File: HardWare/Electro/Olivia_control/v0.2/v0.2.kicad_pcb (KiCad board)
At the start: 2 copper layers, 90 x 100 mm, 49 parts, among them J1 PROG, J10 Motor_B, J11 I2C, J12 DAC, J13 UART2, J14 TRIAC OUT_A, J15 TRIAC OUT_B, J16 220V IN, J17 In12V, J2 Input1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

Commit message: Añadida serigrafía para fabricación industrial.
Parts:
- J17: value In12V -> Input 12Vcc max
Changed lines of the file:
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@@
 		(tags "resistor handsolder")
 		(property "Reference" "R2"
-			(at 0 -1.65 0)
+			(at 0.005398 1.74998 0)
 			(layer "F.SilkS")
 			(effects
@@
 		)
 		(property "Value" "10K"
-			(at 0 1.65 0)
-			(layer "F.Fab")
+			(at -2.576 1.804 0)
+			(layer "F.SilkS")
 			(effects
 				(font
@@
 		(tags "capacitor handsolder")
 		(property "Reference" "C5"
-			(at 0 -1.68 0)
+			(at -1.398 -1.862 0)
 			(layer "F.SilkS")
 			(effects
@@
 		)
 		(property "Value" "100nF"
-			(at 0 1.68 0)
-			(layer "F.Fab")
+			(at -4.954 -1.862 0)
+			(layer "F.SilkS")
 			(effects
 				(font
@@
 		(property "Value" "10uF"
 			(at 0 1.68 0)
-			(layer "F.Fab")
+			(layer "F.SilkS")
 			(effects
 				(font
@@
 		(tags "resistor handsolder")
 		(property "Reference" "R1"
-			(at 0 -1.65 0)
+			(at 0.352 1.648 0)
 			(layer "F.SilkS")
 			(effects
@@
 		)
 		(property "Value" "10K"
-			(at 0 1.65 0)
-			(layer "F.Fab")
+			(at -2.188 1.65 0)
+			(layer "F.SilkS")
 			(effects
 				(font
@@
 		)
 		(property "Value" "100nF"
-			(at -0.0375 -3.25 0)
-			(layer "F.Fab")
+			(at -0.0375 2.026 0)
+			(layer "F.SilkS")
 			(effects
 				(font
@@
 			)
 		)
-		(property "Value" "In12V"
-			(at -6.2 -5.5 90)
-			(layer "F.Fab")
+		(property "Value" "Input 12Vcc max"
+			(at 3.252 -0.316 180)
+			(layer "F.SilkS")
 			(effects
 				(font
@@
 		(property "Value" "10K"
 			(at 0 1.65 0)
-			(layer "F.Fab")
+			(layer "F.SilkS")
 			(effects
 				(font
@@
 		(property "Value" "ESP32-WROOM-32D"
 			(at 0 11.5 0)
-			(layer "F.Fab")
+			(layer "F.SilkS")
 			(effects
 				(font
@@
 		(tags "resistor handsolder")
 		(property "Reference" "R4"
-			(at 0 -1.65 0)
+			(at 0 1.668 0)
 			(layer "F.SilkS")
 			(effects
@@
 		)
 		(property "Value" "10K"
-			(at 0 2 0)
-			(layer "F.Fab")
+			(at -3.0665 1.668 0)
+			(layer "F.SilkS")
 			(effects
 				(font
@@
 		(tags "resistor handsolder")
 		(property "Reference" "R3"
-			(at 0 -1.65 0)
+			(at 0.003171 1.676848 0)
 			(layer "F.SilkS")
 			(effects
@@
 		)
 		(property "Value" "10K"
-			(at 0 1.65 0)
-			(layer "F.Fab")
+			(at -2.596 1.65 0)
+			(layer "F.SilkS")
 			(effects
 				(font
@@
 		(tags "ACDC-Converter 10W THT Hi-Link board mount module")
 		(property "Reference" "PS1"
-			(at -1.3 -12.39 0)
+			(at 38.0285 -12.774 0)
 			(layer "F.SilkS")
 			(effects
@@
 		)
 		(property "Value" "HLK-10M05"
-			(at -8.45 -1.7 0)
-			(layer "F.Fab")
+			(at 31.4245 -12.774 0)
+			(layer "F.SilkS")
 			(effects
 				(font
@@
 		(tags "capacitor handsolder")
 		(property "Reference" "C2"
-			(at 0 -1.68 0)
+			(at -1.498803 -1.68 0)
 			(layer "F.SilkS")
 			(effects
@@
 		)
 		(property "Value" "100nF"
-			(at 0 1.68 0)
-			(layer "F.Fab")
+			(at -5.004 -1.707953 0)
+			(layer "F.SilkS")
 			(effects
 				(font
@@
 		(tags "capacitor handsolder")
 		(property "Reference" "C3"
-			(at 0 -1.68 0)
+			(at -1.68726 -1.792 0)
 			(layer "F.SilkS")
 			(effects
@@
 		)
 		(property "Value" "100nF"
-			(at 0 1.68 0)
-			(layer "F.Fab")
+			(at -5.104 -1.792 0)
+			(layer "F.SilkS")
 			(effects
 				(font
@@
 		(tags "capacitor handsolder")
 		(property "Reference" "C4"
-			(at 0 -1.68 0)
+			(at -1.548 -1.68 0)
 			(layer "F.SilkS")
 			(effects
@@
 		)
 		(property "Value" "100nF"
-			(at 0 1.68 0)
-			(layer "F.Fab")
+			(at -5.104 -1.536 0)
+			(layer "F.SilkS")
 			(effects
 				(font
@@
 		(property "Value" "100nF"
 			(at 0 -1.68 90)
-			(layer "B.Fab")
+			(layer "B.SilkS")
 			(effects
 				(font
@@
 		(property "Value" "220"
 			(at 0 -1.65 0)
-			(layer "B.Fab")
+			(layer "B.SilkS")
 			(effects
 				(font
@@
 		(property "Value" "BTA16-800B"
 			(at 2.54 -2.5 90)
-			(layer "B.Fab")
+			(layer "B.SilkS")
 			(effects
 				(font
@@
 		(property "Value" "LED"
 			(at 2.54 -5.25 90)
-			(layer "B.Fab")
+			(layer "B.SilkS")
 			(effects
 				(font
@@
 		(property "Value" "4N25"
 			(at 0 -4.87 0)
-			(layer "B.Fab")
+			(layer "B.SilkS")
 			(effects
 				(font
@@
 		(property "Value" "BTA16-800B"
 			(at 2.54 -2.5 90)
-			(layer "B.Fab")
+			(layer "B.SilkS")
 			(effects
 				(font
@@
 		)
 		(property "Value" "TRIAC OUT_B"
-			(at 3.81 -11.2 0)
-			(layer "B.Fab")
+			(at 3.302 4.826 0)
+			(layer "B.SilkS")
 			(effects
 				(font
@@
 		)
 		(property "Value" "Input2"
-			(at 1.27 -5.25 90)
-			(layer "B.Fab")
+			(at 1.27 4.7825 90)
+			(layer "B.SilkS")
 			(effects
 				(font
@@
 		(tags "connector Molex SL vertical")
 		(property "Reference" "J11"
-			(at 3.81 3.75 90)
+			(at 6.822 -5.2 90)
 			(layer "B.SilkS")
 			(effects
@@
 		(property "Value" "I2C"
 			(at 3.81 -5.25 90)
-			(layer "B.Fab")
+			(layer "B.SilkS")
 			(effects
 				(font
@@
 		(property "Value" "Motor_A"
 			(at 3.81 -5.25 0)
-			(layer "B.Fab")
+			(layer "B.SilkS")
 			(effects
 				(font
@@
 		)
 		(property "Value" "AMS1117-3.3"
-			(at 0 -4.5 90)
-			(layer "B.Fab")
+			(at 7.0505 0.1065 180)
+			(layer "B.SilkS")
 			(effects
 				(font
@@
 		(property "Value" "220"
 			(at 0 -1.65 0)
-			(layer "B.Fab")
+			(layer "B.SilkS")
 			(effects
 				(font
@@
 		(property "Value" "Motor_B"
 			(at 3.81 -5.25 0)
-			(layer "B.Fab")
+			(layer "B.SilkS")
 			(effects
 				(font
@@
 		)
 		(property "Value" "Input1"
-			(at 1.27 -5.25 90)
-			(layer "B.Fab")
+			(at 0.942 4.8325 90)
+			(layer "B.SilkS")
 			(effects
 				(font
@@
 		(property "Value" "500mA"
 			(at 0 -1.82 90)
-			(layer "B.Fab")
+			(layer "B.SilkS")
 			(effects
 				(font
@@
 		)
 		(property "Value" "100nF"
-			(at 0 -1.68 0)
-			(layer "B.Fab")
+			(at 0 3.048 0)
+			(layer "B.SilkS")
 			(effects
 				(font
@@
 		)
 		(property "Value" "220V IN"
-			(at 3.81 -11.2 0)
-			(layer "B.Fab")
+			(at 3.805 4.826 0)
+			(layer "B.SilkS")
 			(effects
 				(font
@@
 		)
 		(property "Value" "Input4"
-			(at 1.27 -5.25 90)
-			(layer "B.Fab")
+			(at 0.832 4.82 90)
+			(layer "B.SilkS")
 			(effects
 				(font
@@
 		(property "Value" "120K"
 			(at 0 -1.65 90)
-			(layer "B.Fab")
+			(layer "B.SilkS")
 			(effects
 				(font
@@
 		)
 		(property "Value" "Input3"
-			(at 1.27 -5.25 90)
-			(layer "B.Fab")
+			(at 1.038 4.8325 90)
+			(layer "B.SilkS")
 			(effects
 				(font
@@
 		(property "Value" "1K"
 			(at 0 -1.65 90)
-			(layer "B.Fab")
+			(layer "B.SilkS")
 			(effects
 				(font
@@
 		(property "Value" "10K"
 			(at 0 -1.65 0)
-			(layer "B.Fab")
+			(layer "B.SilkS")
 			(effects
 				(font
@@
 		)
 		(property "Value" "DB107S"
-			(at -0.530597 -7.607962 90)
-			(layer "B.Fab")
+			(at -0.012599 -5.842 90)
+			(layer "B.SilkS")
 			(effects
 				(font
@@
 		(property "Value" "MOC3041M"
 			(at 0 -4.87 90)
-			(layer "B.Fab")
+			(layer "B.SilkS")
 			(effects
 				(font
@@
 		(property "Value" "1K"
 			(at 0 -1.65 90)
-			(layer "B.Fab")
-			(hide yes)
+			(layer "B.SilkS")
 			(effects
 				(font
@@
 		(property "Value" "DAC"
 			(at 2.54 -5.25 90)
-			(layer "B.Fab")
+			(layer "B.SilkS")
 			(effects
 				(font
@@
 		)
 		(property "Value" "TRIAC OUT_A"
-			(at 3.81 -11.2 0)
-			(layer "B.Fab")
+			(at 4.064 4.826 0)
+			(layer "B.SilkS")
 			(effects
 				(font
@@
 		(property "Value" "MOC3041M"
 			(at 0 -4.87 90)
-			(layer "B.Fab")
+			(layer "B.SilkS")
 			(effects
 				(font
@@
 		)
 		(property "Value" "PROG"
-			(at 1.27 -7.41 90)
-			(layer "B.Fab")
+			(at 1.576158 -7.639089 90)
+			(layer "B.SilkS")
 			(effects
 				(font
@@
 		)
 		(property "Value" "Reset"
-			(at 0 3.96 90)
-			(layer "B.Fab")
+			(at 0 -5.282 90)
+			(layer "B.SilkS")
 			(effects
 				(font
@@
 		(property "Value" "UART2"
 			(at 2.54 -5.25 90)
-			(layer "B.Fab")
+			(layer "B.SilkS")
 			(effects
 				(font
@@
 		)
 		(property "Value" "SPI"
-			(at 0 -15.03 0)
-			(layer "B.Fab")
+			(at 0 -15.344 0)
+			(layer "B.SilkS")
 			(effects
 				(font
@@
 		(property "Value" "47uFxx35V"
 			(at 0 -2.55 0)
-			(layer "B.Fab")
+			(layer "B.SilkS")
 			(effects
 				(font
@@
 		)
 		(property "Value" "22uFx16V"
-			(at 0 -2.55 90)
-			(layer "B.Fab")
+			(at -5.0265 0.0735 180)
+			(layer "B.SilkS")
 			(effects
 				(font

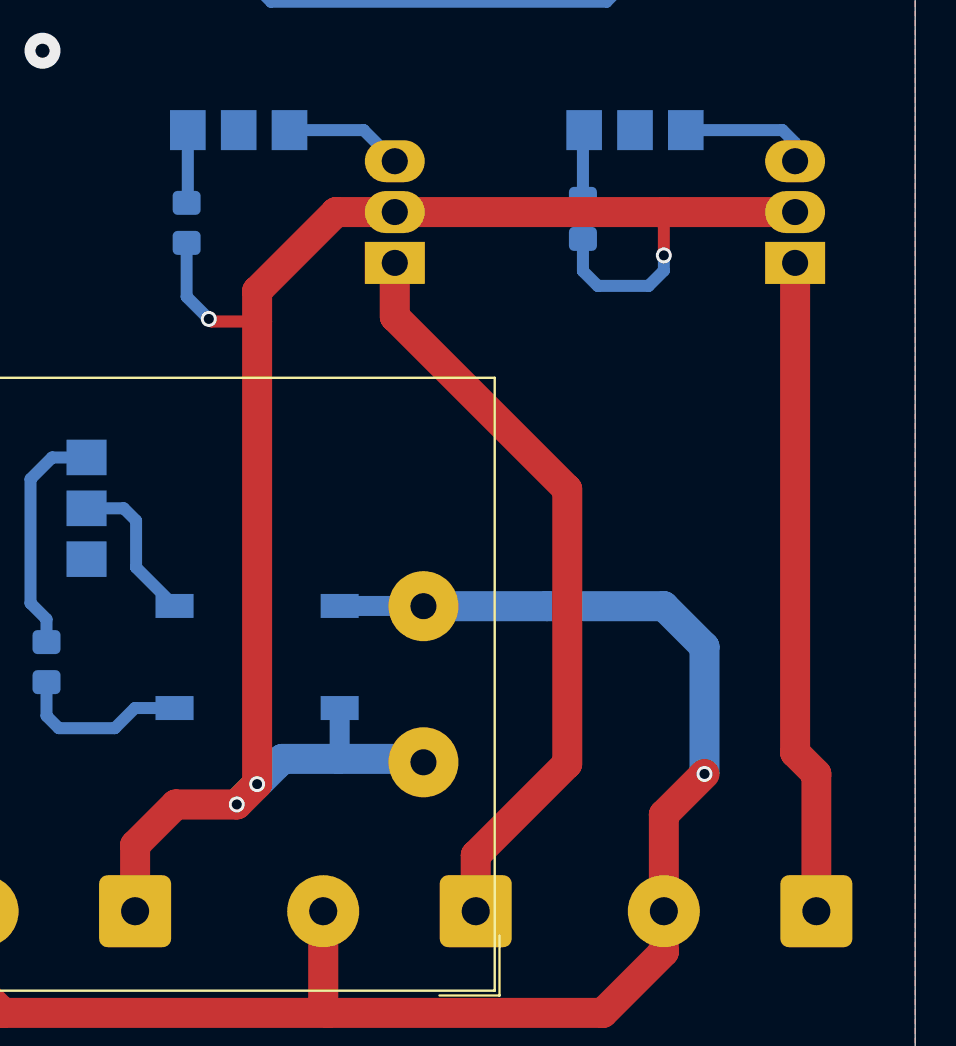
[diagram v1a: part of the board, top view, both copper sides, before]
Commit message: Pequenos fixes en sector 220V. Imagenes de vista, Gerbers y pdf de esquematico generados. Limpieza.
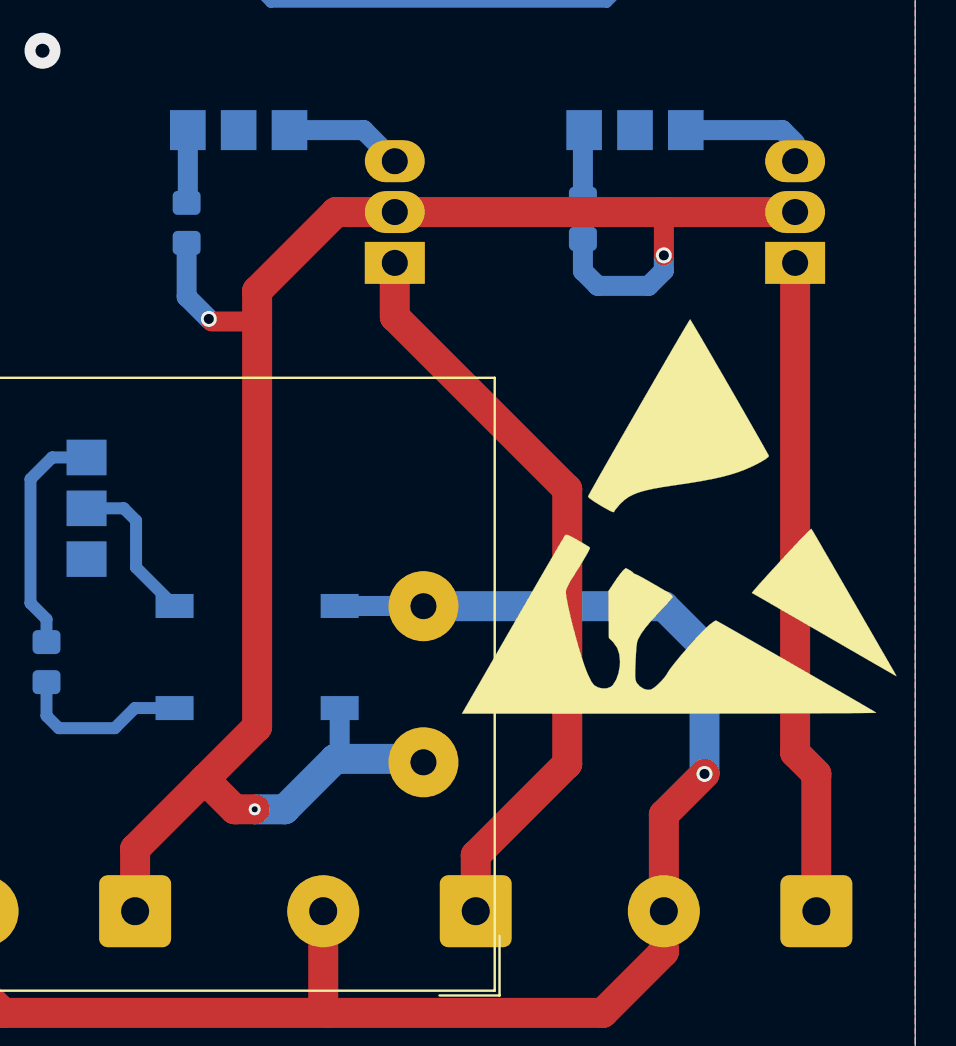
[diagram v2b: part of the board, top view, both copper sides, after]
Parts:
- added REF**: ESD-Logo_22x20mm_SilkScreen, Symbol:ESD-Logo_22x20mm_SilkScreen, F.Cu at (108.2, 128.8)
- added REF**: ESD-Logo_22x20mm_SilkScreen, Symbol:ESD-Logo_22x20mm_SilkScreen, B.Cu at (108.0, 129.0)
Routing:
- net /FASE: track 92.6 -> 93.2 mm, vias 4 -> 3
